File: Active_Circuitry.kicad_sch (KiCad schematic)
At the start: 22 parts, among them J1 2Pin_Header_2.54, U1 CEC1702, U1 SST25VF040B-50-4C-SAF-T, U3 TXB0104PWR, Y1 32.768kHz

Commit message: updated pcb, schematic, production files
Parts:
- removed R5: DNM_0603, Resistor_SMD:R_0603_1608Metric, symbol tutorial_2_library:DNM_RES_0603_1
- removed SJ1: ~, Jumper:SolderJumper-2_P1.3mm_Bridged2Bar_Pad1.0x1.5mm, symbol tutorial_2_library:Solder_Jumper_2_NC
- removed U1: SST25VF040B-50-4C-SAF-T, Package_SO:SOIC-8_5.275x5.275mm_P1.27mm, symbol tutorial_2_library:SST25VF040B-50-4C-SAF-T
- added JP1: ~, Jumper:SolderJumper-2_P1.3mm_Bridged2Bar_Pad1.0x1.5mm, symbol tutorial_2_library:Solder_Jumper_2_NC
- added PCB1: CE Symbol, Silkscrren_Symbols:CE-Logo_8.5x6mm_SilkScreen, symbol Silkscreen_Symbols:CE_Free
- added PCB2: Pb_Free Symbol, Silkscrren_Symbols:Pb_Free_8.0x8.0mm_SilkScreen, symbol Silkscreen_Symbols:Pb_Free
- added PCB3: UKCA symbol, Silkscrren_Symbols:UKCA-Logo_8x8mm_SilkScreen, symbol Silkscreen_Symbols:UKCA
- added PCB4: WEEE SYMBOL, Silkscrren_Symbols:WEEE-Logo_5.6x8mm_SilkScreen, symbol Silkscreen_Symbols:WEEE
- added R5: RES_100R_0603, Resistor_SMD:R_0603_1608Metric, symbol 0603_Yageo_Res:RES_100R_0603
- added U2: SST26VF016B-104I/SN, Package_SO:SOIC-8_3.9x4.9mm_P1.27mm, symbol tutorial_2_library:SST26VF016B
- renumbered R11 to R9
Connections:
- net FLASH_SIO2 is gone; now on net FLASH_CS: R3.1, U1.K4 (GPIO227/QSPI0_IO2)
- net +3V3: now also J1.2, R4.1, U2.8 (VDD); no longer J1., R4.2
- net CLK_IN: now also JP1.1
- net FLASH_CS: now also U2.1 (CE#), U2.3 (WP#/SIO2)
- net FLASH_SCK: now also U2.6 (SCK)
- net FLASH_SIO0: now also U2.5 (SI/SIO0)
- net FLASH_SIO1: now also U2.2 (SO/SIO1)
- net FLASH_SIO3: now also R4.2, U2.7 (HOLD/SIO3); no longer R4.1
- net GND: now also U2.4 (VSS)
- net at C2.1, U1.A2 (XTAL2), Y1.2: now also R5.1
- net at R8.1: now also JP1.2, R5.2
- net at C14.2, U1.E3 (VREF_ADC): now also J1.1; no longer J1.
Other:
- note added: "Oscillating crystal circuit left in for now - most likely will not be mounted"
- moved on the sheet: C14, R4, R7

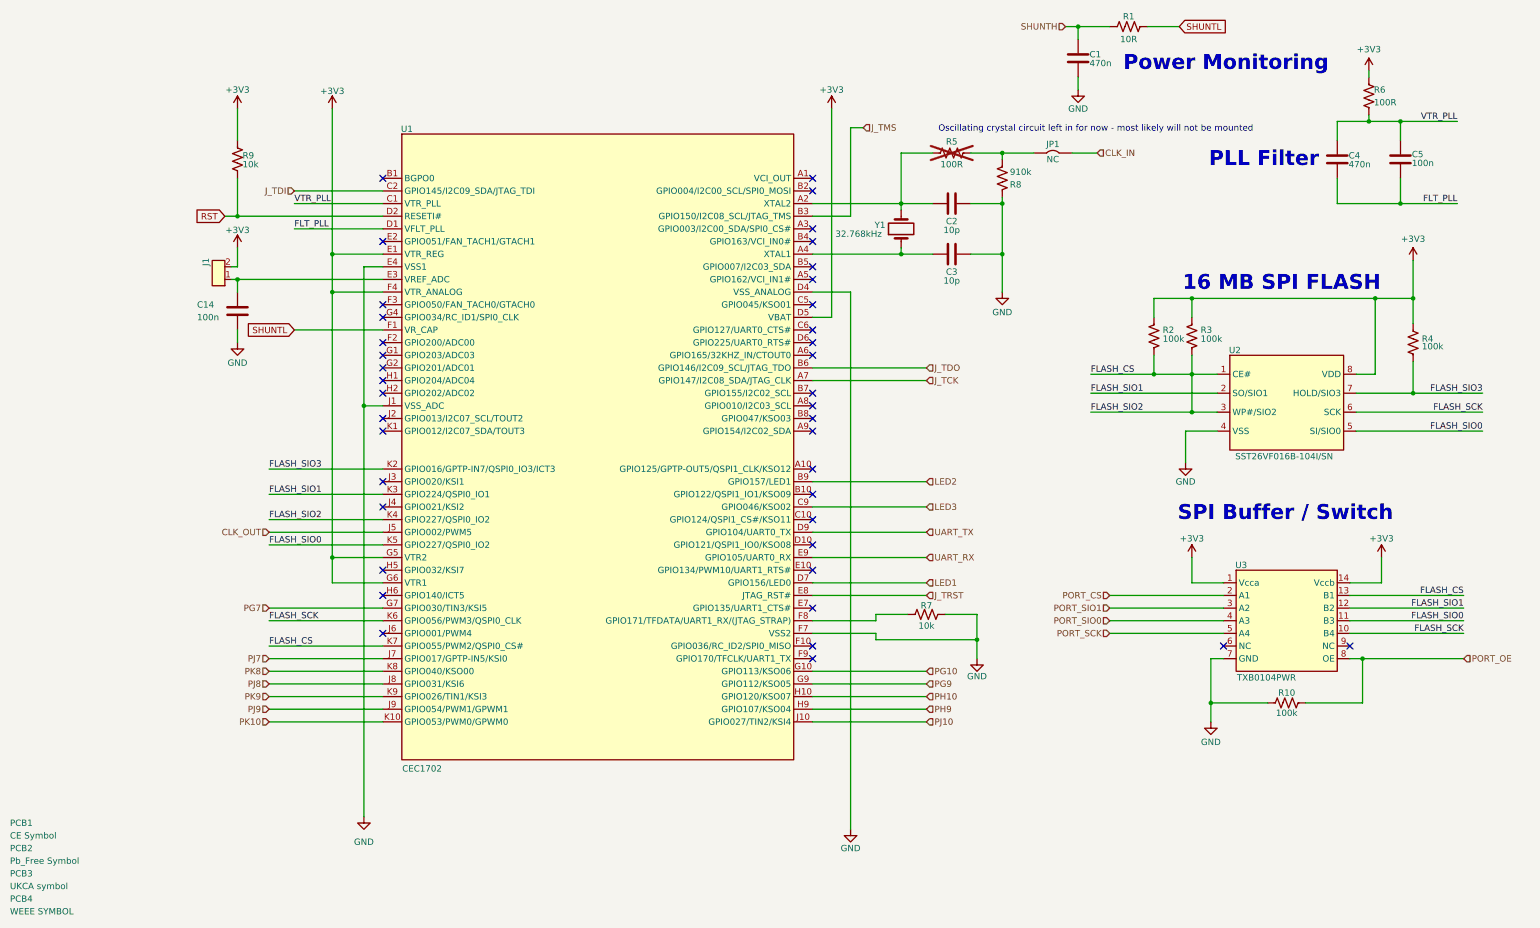
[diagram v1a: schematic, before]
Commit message: updated schematic and pcb after library re-organization
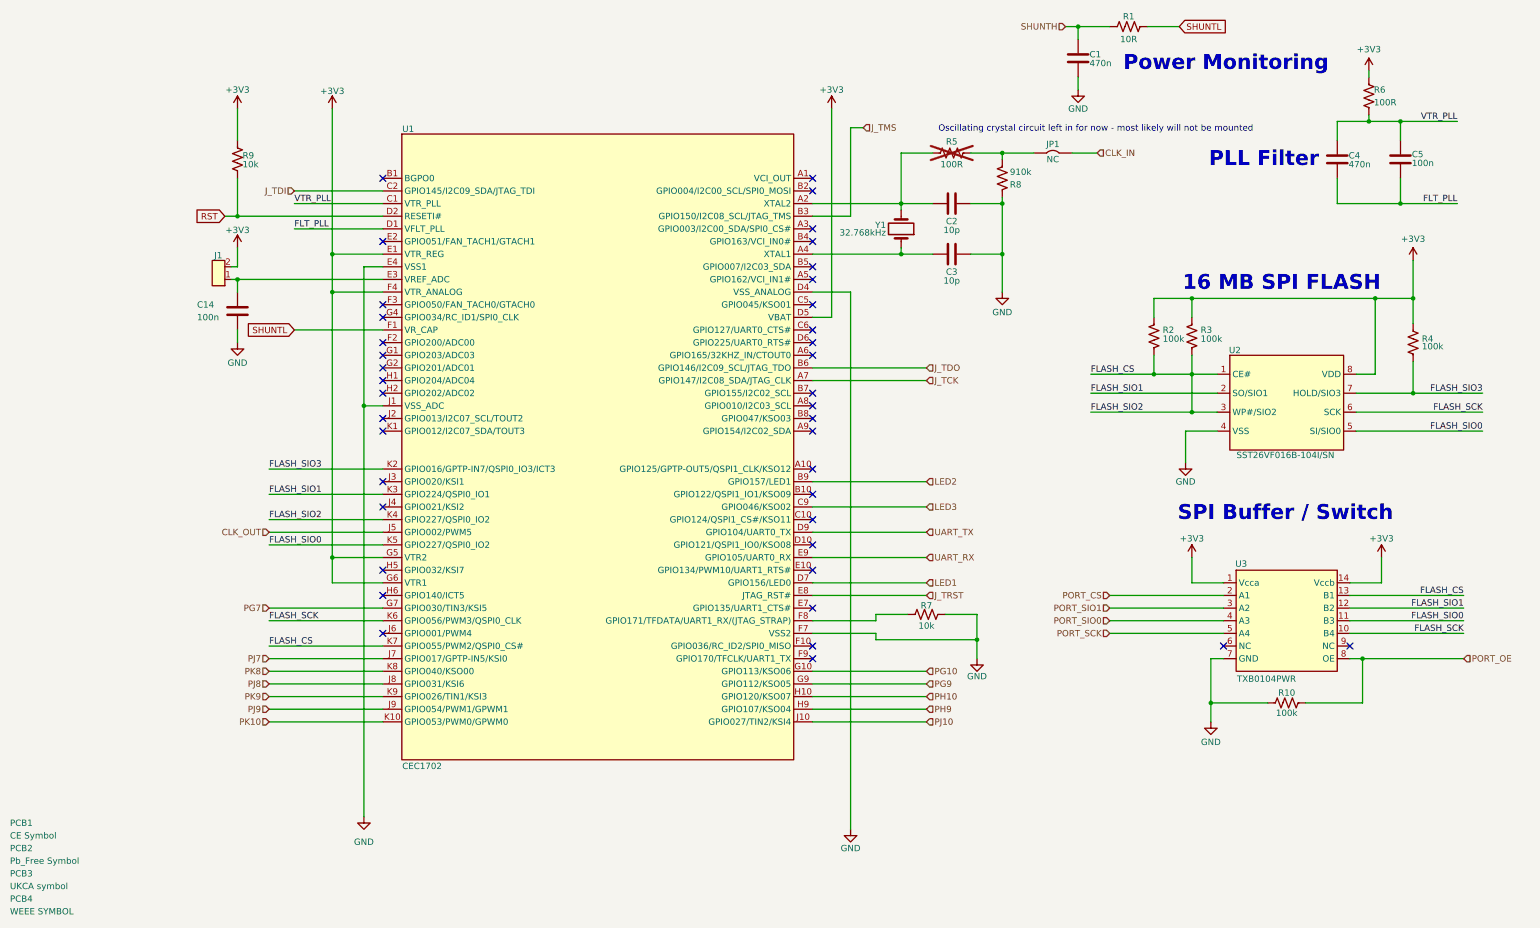
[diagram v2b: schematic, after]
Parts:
- removed J1: 2Pin_Header_2.54, Connector_PinHeader_2.54mm:PinHeader_2x01_P2.54mm_Vertical, symbol tutorial_2_library:HEADER_2_2.54MM
- removed JP1: ~, Jumper:SolderJumper-2_P1.3mm_Bridged2Bar_Pad1.0x1.5mm, symbol tutorial_2_library:Solder_Jumper_2_NC
- removed U1: CEC1702, tutorial_2_library:BGA84C65P10X10_700X700X80, symbol tutorial_2_library:CEC1702
- removed U2: SST26VF016B-104I/SN, Package_SO:SOIC-8_3.9x4.9mm_P1.27mm, symbol tutorial_2_library:SST26VF016B
- removed U3: TXB0104PWR, Package_SO:SOIC-14_3.9x8.7mm_P1.27mm, symbol tutorial_2_library:TXB0104PWR
- removed Y1: 32.768kHz, Crystal:Crystal_SMD_3215-2Pin_3.2x1.5mm, symbol tutorial_2_library:32.768kHz
- added J1: 2Pin_Header_2.54, Connector_PinHeader_2.54mm:PinHeader_2x01_P2.54mm_Vertical, symbol NAE_Connectors:VERT_HDR_2_2.54mm
- added JP1: ~, Jumper:SolderJumper-2_P1.3mm_Bridged2Bar_Pad1.0x1.5mm, symbol NAE_Connectors:Solder_Jumper_2_NC
- added U1: CEC1702, tutorial_2_library:BGA84C65P10X10_700X700X80, symbol NAE_Integrated_Circuits:CEC1702
- added U2: SST26VF016B-104I/SN, Package_SO:SOIC-8_3.9x4.9mm_P1.27mm, symbol NAE_Integrated_Circuits:SST26VF016B
- added U3: TXB0104PWR, Package_SO:SOIC-14_3.9x8.7mm_P1.27mm, symbol NAE_Integrated_Circuits:TXB0104PWR
- added Y1: 32.768kHz, Crystal:Crystal_SMD_3215-2Pin_3.2x1.5mm, symbol NAE_Crystals:Crystal_32.768kHz_SMD
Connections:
- net +3V3: now also J1.2, U1.D5 (VBAT), U1.E1 (VTR_REG), U1.F4 (VTR_ANALOG), U1.G5 (VTR2), U1.G6 (VTR1), U2.8 (VDD), U3.1 (Vcca), U3.14 (Vccb)
- net CLK_IN: now also JP1.1
- net CLK_OUT: now also U1.J5 (GPIO002/PWM5)
- net FLASH_CS: now also U1.K4 (GPIO227/QSPI0_IO2), U1.K7 (GPIO055/PWM2/QSPI0_CS#), U2.1 (CE#), U2.3 (WP#/SIO2), U3.13 (B1)
- net FLASH_SCK: now also U1.K6 (GPIO056/PWM3/QSPI0_CLK), U2.6 (SCK), U3.10 (B4)
- net FLASH_SIO0: now also U1.K5 (GPIO227/QSPI0_IO2), U2.5 (SI/SIO0), U3.11 (B3)
- net FLASH_SIO1: now also U1.K3 (GPIO224/QSPI0_IO1), U2.2 (SO/SIO1), U3.12 (B2)
- net FLASH_SIO3: now also U1.K2 (GPIO016/GPTP-IN7/QSPI0_IO3/ICT3), U2.7 (HOLD/SIO3)
- net FLT_PLL: now also U1.D1 (VFLT_PLL)
- net GND: now also U1.D4 (VSS_ANALOG), U1.E4 (VSS1), U1.F7 (VSS2), U1.J1 (VSS_ADC), U2.4 (VSS), U3.7 (GND)
- net J_TCK: now also U1.A7 (GPIO147/I2C08_SDA/JTAG_CLK)
- net J_TDI: now also U1.C2 (GPIO145/I2C09_SDA/JTAG_TDI)
- net J_TDO: now also U1.B6 (GPIO146/I2C09_SCL/JTAG_TDO)
- net J_TMS: now also U1.B3 (GPIO150/I2C08_SCL/JTAG_TMS)
- net J_TRST: now also U1.E8 (JTAG_RST#)
- net LED1: now also U1.D7 (GPIO156/LED0)
- net LED2: now also U1.B9 (GPIO157/LED1)
- net LED3: now also U1.C9 (GPIO046/KSO02)
- net PG10: now also U1.G10 (GPIO113/KSO06)
- net PG7: now also U1.G7 (GPIO030/TIN3/KSI5)
- net PG9: now also U1.G9 (GPIO112/KSO05)
- net PH10: now also U1.H10 (GPIO120/KSO07)
- net PH9: now also U1.H9 (GPIO107/KSO04)
- net PJ10: now also U1.J10 (GPIO027/TIN2/KSI4)
- net PJ7: now also U1.J7 (GPIO017/GPTP-IN5/KSI0)
- net PJ8: now also U1.J8 (GPIO031/KSI6)
- net PJ9: now also U1.J9 (GPIO054/PWM1/GPWM1)
- net PK10: now also U1.K10 (GPIO053/PWM0/GPWM0)
- net PK8: now also U1.K8 (GPIO040/KSO00)
- net PK9: now also U1.K9 (GPIO026/TIN1/KSI3)
- net PORT_CS: now also U3.2 (A1)
- net PORT_OE: now also U3.8 (OE)
- net PORT_SCK: now also U3.5 (A4)
- net PORT_SIO0: now also U3.4 (A3)
- net PORT_SIO1: now also U3.3 (A2)
- net RST: now also U1.D2 (RESETI#)
- net SHUNTL: now also U1.F1 (VR_CAP)
- net UART_RX: now also U1.E9 (GPIO105/UART0_RX)
- net UART_TX: now also U1.D9 (GPIO104/UART0_TX)
- net VTR_PLL: now also U1.C1 (VTR_PLL)
- net at R5.2, R8.1: now also JP1.2
- net at C14.2: now also J1.1, U1.E3 (VREF_ADC)
- net at C3.1: now also U1.A4 (XTAL1), Y1.1
- net at C2.1, R5.1: now also U1.A2 (XTAL2), Y1.2
- net at R7.1: now also U1.F8 (GPIO171/TFDATA/UART1_RX/(JTAG_STRAP))
